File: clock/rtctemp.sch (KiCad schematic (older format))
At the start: 17 parts, among them U601 ADT7410, U602 DS3231, U603 ADT7410

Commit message: Checkpoint layout. Update hand soldering footprints for 0805 parts.
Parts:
- C601, C602, C603: footprint Capacitors_SMD:C_0805_HandSoldering -> local:C_0805_HandSoldering
- R601, R602, R603, R604, R605, R606, R607, R608, R609, R610: footprint Resistors_SMD:R_0805_HandSoldering -> local:R_0805_HandSoldering
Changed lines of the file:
@@
 F 0 "R603" V 4130 2050 50  0000 C CNN
 F 1 "1.00K" V 3975 2050 50  0000 C CNN
-F 2 "Resistors_SMD:R_0805_HandSoldering" V 3980 2050 30  0001 C CNN
+F 2 "local:R_0805_HandSoldering" V 3980 2050 30  0001 C CNN
 F 3 "" V 4130 2050 30  0000 C CNN
 F 4 "1%" V 3900 2050 50  0000 C CNN "Tolerance"
@@
 F 0 "R604" V 4580 2050 50  0000 C CNN
 F 1 "1.00K" V 4425 2050 50  0000 C CNN
-F 2 "Resistors_SMD:R_0805_HandSoldering" V 4430 2050 30  0001 C CNN
+F 2 "local:R_0805_HandSoldering" V 4430 2050 30  0001 C CNN
 F 3 "" V 4580 2050 30  0000 C CNN
 F 4 "1%" V 4350 2050 50  0000 C CNN "Tolerance"
@@
 F 0 "R605" V 5630 4250 50  0000 C CNN
 F 1 "1.00K" V 5475 4250 50  0000 C CNN
-F 2 "Resistors_SMD:R_0805_HandSoldering" V 5480 4250 30  0001 C CNN
+F 2 "local:R_0805_HandSoldering" V 5480 4250 30  0001 C CNN
 F 3 "" V 5630 4250 30  0000 C CNN
 F 4 "1%" V 5400 4250 50  0000 C CNN "Tolerance"
@@
 F 0 "R606" V 6080 4250 50  0000 C CNN
 F 1 "1.00K" V 5925 4250 50  0000 C CNN
-F 2 "Resistors_SMD:R_0805_HandSoldering" V 5930 4250 30  0001 C CNN
+F 2 "local:R_0805_HandSoldering" V 5930 4250 30  0001 C CNN
 F 3 "" V 6080 4250 30  0000 C CNN
 F 4 "1%" V 5850 4250 50  0000 C CNN "Tolerance"
@@
 F 0 "R601" V 3180 5300 50  0000 C CNN
 F 1 "1.00K" V 3025 5300 50  0000 C CNN
-F 2 "Resistors_SMD:R_0805_HandSoldering" V 3030 5300 30  0001 C CNN
+F 2 "local:R_0805_HandSoldering" V 3030 5300 30  0001 C CNN
 F 3 "" V 3180 5300 30  0000 C CNN
 F 4 "1%" V 2950 5300 50  0000 C CNN "Tolerance"
@@
 F 0 "R602" V 3630 5300 50  0000 C CNN
 F 1 "1.00K" V 3475 5300 50  0000 C CNN
-F 2 "Resistors_SMD:R_0805_HandSoldering" V 3480 5300 30  0001 C CNN
+F 2 "local:R_0805_HandSoldering" V 3480 5300 30  0001 C CNN
 F 3 "" V 3630 5300 30  0000 C CNN
 F 4 "1%" V 3400 5300 50  0000 C CNN "Tolerance"
@@
 F 0 "R608" V 6530 5300 50  0000 C CNN
 F 1 "1.00K" V 6375 5300 50  0000 C CNN
-F 2 "Resistors_SMD:R_0805_HandSoldering" V 6380 5300 30  0001 C CNN
+F 2 "local:R_0805_HandSoldering" V 6380 5300 30  0001 C CNN
 F 3 "" V 6530 5300 30  0000 C CNN
 F 4 "1%" V 6300 5300 50  0000 C CNN "Tolerance"
@@
 F 0 "R607" V 6530 4250 50  0000 C CNN
 F 1 "1.00K" V 6375 4250 50  0000 C CNN
-F 2 "Resistors_SMD:R_0805_HandSoldering" V 6380 4250 30  0001 C CNN
+F 2 "local:R_0805_HandSoldering" V 6380 4250 30  0001 C CNN
 F 3 "" V 6530 4250 30  0000 C CNN
 F 4 "1%" V 6300 4250 50  0000 C CNN "Tolerance"
@@
 F 0 "C603" H 8575 2600 50  0000 L CNN
 F 1 "0.1uF" H 8575 2400 50  0000 L CNN
-F 2 "Capacitors_SMD:C_0805_HandSoldering" H 8588 2350 30  0001 C CNN
+F 2 "local:C_0805_HandSoldering" H 8588 2350 30  0001 C CNN
 F 3 "" H 8550 2500 60  0000 C CNN
 F 4 "50V" H 8450 2400 50  0000 C CNN "Voltage"
@@
 F 0 "C601" H 4175 6450 50  0000 L CNN
 F 1 "0.1uF" H 4175 6250 50  0000 L CNN
-F 2 "Capacitors_SMD:C_0805_HandSoldering" H 4188 6200 30  0001 C CNN
+F 2 "local:C_0805_HandSoldering" H 4188 6200 30  0001 C CNN
 F 3 "" H 4150 6350 60  0000 C CNN
 F 4 "50V" H 4050 6250 50  0000 C CNN "Voltage"
@@
 F 0 "C602" H 6175 6450 50  0000 L CNN
 F 1 "0.1uF" H 6175 6250 50  0000 L CNN
-F 2 "Capacitors_SMD:C_0805_HandSoldering" H 6188 6200 30  0001 C CNN
+F 2 "local:C_0805_HandSoldering" H 6188 6200 30  0001 C CNN
 F 3 "" H 6150 6350 60  0000 C CNN
 F 4 "50V" H 6050 6250 50  0000 C CNN "Voltage"
@@
 F 0 "R609" V 6580 1450 50  0000 C CNN
 F 1 "10.0K" V 6425 1450 50  0000 C CNN
-F 2 "Resistors_SMD:R_0805_HandSoldering" V 6430 1450 30  0001 C CNN
+F 2 "local:R_0805_HandSoldering" V 6430 1450 30  0001 C CNN
 F 3 "" V 6580 1450 30  0000 C CNN
 F 4 "1%" V 6350 1450 50  0000 C CNN "Tolerance"
@@
 F 0 "R610" V 7130 1450 50  0000 C CNN
 F 1 "10.0K" V 6975 1450 50  0000 C CNN
-F 2 "Resistors_SMD:R_0805_HandSoldering" V 6980 1450 30  0001 C CNN
+F 2 "local:R_0805_HandSoldering" V 6980 1450 30  0001 C CNN
 F 3 "" V 7130 1450 30  0000 C CNN
 F 4 "1%" V 6900 1450 50  0000 C CNN "Tolerance"

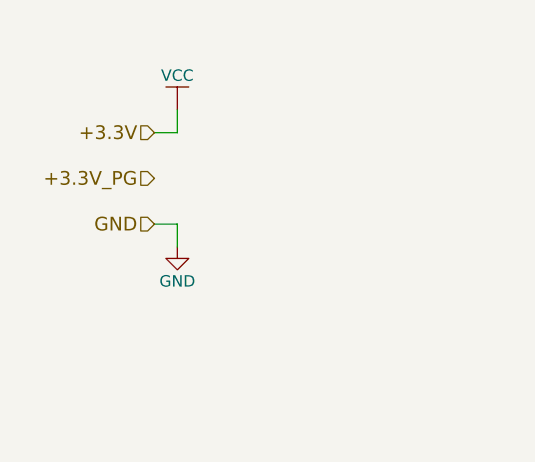
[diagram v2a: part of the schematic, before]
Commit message: Remove sheet to sheet power interconnect because power symbols are global.
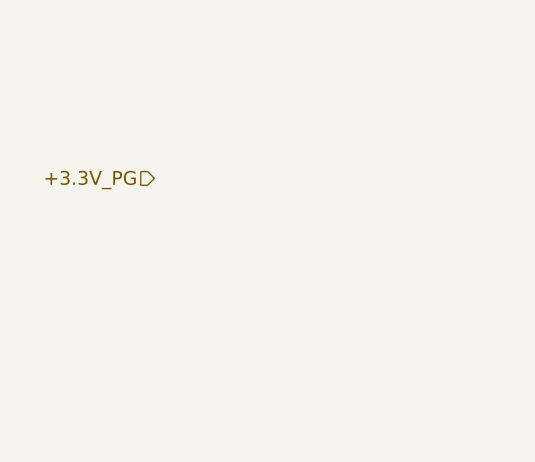
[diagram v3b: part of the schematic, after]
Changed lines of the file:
@@
 	1    0    0    -1
 $EndComp
-Text HLabel 1350 1400 0    60   Input ~ 0
-+3.3V
 Text HLabel 1350 1600 0    60   Input ~ 0
 +3.3V_PG
-Text HLabel 1350 1800 0    60   Input ~ 0
-GND
 Text HLabel 3650 2350 0    60   Input ~ 0
 RTC_SCL
 Text HLabel 3650 2450 0    60   Input ~ 0
 RTC_SDA
-$Comp
-L GND #PWR083
-U 1 1 5636B600
-P 1450 1900
-F 0 "#PWR083" H 1450 1650 50  0001 C CNN
-F 1 "GND" H 1450 1750 50  0000 C CNN
-F 2 "" H 1450 1900 60  0000 C CNN
-F 3 "" H 1450 1900 60  0000 C CNN
-	1    1450 1900
-	1    0    0    -1
-$EndComp
-Wire Wire Line
-	1350 1800 1450 1800
-Wire Wire Line
-	1450 1800 1450 1900
 Wire Wire Line
 	5750 3400 5750 3300
 $Comp
-L GND #PWR084
+L GND #PWR081
 U 1 1 5636B6C4
 P 5750 3400
-F 0 "#PWR084" H 5750 3150 50  0001 C CNN
+F 0 "#PWR081" H 5750 3150 50  0001 C CNN
 F 1 "GND" H 5750 3250 50  0000 C CNN
 F 2 "" H 5750 3400 60  0000 C CNN
@@
 $EndComp
 $Comp
-L VCC #PWR085
-U 1 1 5636B791
-P 1450 1300
-F 0 "#PWR085" H 1450 1150 50  0001 C CNN
-F 1 "VCC" H 1450 1450 50  0000 C CNN
-F 2 "" H 1450 1300 60  0000 C CNN
-F 3 "" H 1450 1300 60  0000 C CNN
-	1    1450 1300
-	1    0    0    -1
-$EndComp
-Wire Wire Line
-	1350 1400 1450 1400
-Wire Wire Line
-	1450 1400 1450 1300
-$Comp
-L VCC #PWR086
+L VCC #PWR082
 U 1 1 5636B7D2
 P 5750 2000
-F 0 "#PWR086" H 5750 1850 50  0001 C CNN
+F 0 "#PWR082" H 5750 1850 50  0001 C CNN
 F 1 "VCC" H 5750 2150 50  0000 C CNN
 F 2 "" H 5750 2000 60  0000 C CNN
@@
 	4500 1800 4500 1900
 $Comp
-L VCC #PWR087
+L VCC #PWR083
 U 1 1 5636BBAE
 P 4300 1700
-F 0 "#PWR087" H 4300 1550 50  0001 C CNN
+F 0 "#PWR083" H 4300 1550 50  0001 C CNN
 F 1 "VCC" H 4300 1850 50  0000 C CNN
 F 2 "" H 4300 1700 60  0000 C CNN
@@
 	6950 2550 6950 2650
 $Comp
-L GND #PWR088
+L GND #PWR084
 U 1 1 5636BC94
 P 6950 3050
-F 0 "#PWR088" H 6950 2800 50  0001 C CNN
+F 0 "#PWR084" H 6950 2800 50  0001 C CNN
 F 1 "GND" H 6950 2900 50  0000 C CNN
 F 2 "" H 6950 3050 60  0000 C CNN
@@
 $EndComp
 $Comp
-L VCC #PWR089
+L VCC #PWR085
 U 1 1 5636C0D5
 P 4200 4150
-F 0 "#PWR089" H 4200 4000 50  0001 C CNN
+F 0 "#PWR085" H 4200 4000 50  0001 C CNN
 F 1 "VCC" H 4200 4300 50  0000 C CNN
 F 2 "" H 4200 4150 60  0000 C CNN
@@
 	7100 5350 7100 5250
 $Comp
-L GND #PWR090
+L GND #PWR086
 U 1 1 5636C104
 P 7100 5350
-F 0 "#PWR090" H 7100 5100 50  0001 C CNN
+F 0 "#PWR086" H 7100 5100 50  0001 C CNN
 F 1 "GND" H 7100 5200 50  0000 C CNN
 F 2 "" H 7100 5350 60  0000 C CNN
@@
 	4200 5350 4200 5250
 $Comp
-L GND #PWR091
+L GND #PWR087
 U 1 1 5636C11B
 P 4200 5350
-F 0 "#PWR091" H 4200 5100 50  0001 C CNN
+F 0 "#PWR087" H 4200 5100 50  0001 C CNN
 F 1 "GND" H 4200 5200 50  0000 C CNN
 F 2 "" H 4200 5350 60  0000 C CNN
@@
 	6000 4000 6000 4100
 $Comp
-L VCC #PWR092
+L VCC #PWR088
 U 1 1 5636C1AA
 P 5800 3900
-F 0 "#PWR092" H 5800 3750 50  0001 C CNN
+F 0 "#PWR088" H 5800 3750 50  0001 C CNN
 F 1 "VCC" H 5800 4050 50  0000 C CNN
 F 2 "" H 5800 3900 60  0000 C CNN
@@
 Connection ~ 3550 5550
 $Comp
-L GND #PWR093
+L GND #PWR089
 U 1 1 5636C550
 P 3550 5650
-F 0 "#PWR093" H 3550 5400 50  0001 C CNN
+F 0 "#PWR089" H 3550 5400 50  0001 C CNN
 F 1 "GND" H 3550 5500 50  0000 C CNN
 F 2 "" H 3550 5650 60  0000 C CNN
@@
 	6450 4950 6450 5150
 $Comp
-L GND #PWR094
+L GND #PWR090
 U 1 1 5636C5CD
 P 6450 5550
-F 0 "#PWR094" H 6450 5300 50  0001 C CNN
+F 0 "#PWR090" H 6450 5300 50  0001 C CNN
 F 1 "GND" H 6450 5400 50  0000 C CNN
 F 2 "" H 6450 5550 60  0000 C CNN
@@
 Connection ~ 3500 4650
 $Comp
-L GND #PWR095
+L GND #PWR091
 U 1 1 5636CF30
 P 8550 2750
-F 0 "#PWR095" H 8550 2500 50  0001 C CNN
+F 0 "#PWR091" H 8550 2500 50  0001 C CNN
 F 1 "GND" H 8550 2600 50  0000 C CNN
 F 2 "" H 8550 2750 60  0000 C CNN
@@
 $EndComp
 $Comp
-L VCC #PWR096
+L VCC #PWR092
 U 1 1 5636D2DE
 P 8550 2250
-F 0 "#PWR096" H 8550 2100 50  0001 C CNN
+F 0 "#PWR092" H 8550 2100 50  0001 C CNN
 F 1 "VCC" H 8550 2400 50  0000 C CNN
 F 2 "" H 8550 2250 60  0000 C CNN
@@
 $EndComp
 $Comp
-L GND #PWR097
+L GND #PWR093
 U 1 1 5636D43C
 P 4150 6600
-F 0 "#PWR097" H 4150 6350 50  0001 C CNN
+F 0 "#PWR093" H 4150 6350 50  0001 C CNN
 F 1 "GND" H 4150 6450 50  0000 C CNN
 F 2 "" H 4150 6600 60  0000 C CNN
@@
 $EndComp
 $Comp
-L VCC #PWR098
+L VCC #PWR094
 U 1 1 5636D44F
 P 4150 6100
-F 0 "#PWR098" H 4150 5950 50  0001 C CNN
+F 0 "#PWR094" H 4150 5950 50  0001 C CNN
 F 1 "VCC" H 4150 6250 50  0000 C CNN
 F 2 "" H 4150 6100 60  0000 C CNN
@@
 $EndComp
 $Comp
-L GND #PWR099
+L GND #PWR095
 U 1 1 5636D49F
 P 6150 6600
-F 0 "#PWR099" H 6150 6350 50  0001 C CNN
+F 0 "#PWR095" H 6150 6350 50  0001 C CNN
 F 1 "GND" H 6150 6450 50  0000 C CNN
 F 2 "" H 6150 6600 60  0000 C CNN
@@
 $EndComp
 $Comp
-L VCC #PWR0100
+L VCC #PWR096
 U 1 1 5636D4B2
 P 6150 6100
-F 0 "#PWR0100" H 6150 5950 50  0001 C CNN
+F 0 "#PWR096" H 6150 5950 50  0001 C CNN
 F 1 "VCC" H 6150 6250 50  0000 C CNN
 F 2 "" H 6150 6100 60  0000 C CNN
@@
 NoConn ~ 5150 2550
 $Comp
-L VCC #PWR0101
+L VCC #PWR097
 U 1 1 563E1DA8
 P 7100 4150
-F 0 "#PWR0101" H 7100 4000 50  0001 C CNN
+F 0 "#PWR097" H 7100 4000 50  0001 C CNN
 F 1 "VCC" H 7100 4300 50  0000 C CNN
 F 2 "" H 7100 4150 60  0000 C CNN
@@
 	6450 5550 6450 5450
 $Comp
-L PWR_FLAG #FLG0102
+L PWR_FLAG #FLG098
 U 1 1 564556C2
 P 7300 2450
-F 0 "#FLG0102" H 7300 2545 50  0001 C CNN
+F 0 "#FLG098" H 7300 2545 50  0001 C CNN
 F 1 "PWR_FLAG" H 7300 2630 50  0000 C CNN
 F 2 "" H 7300 2450 60  0000 C CNN
@@
 Connection ~ 6500 1700
 $Comp
-L VCC #PWR0103
+L VCC #PWR099
 U 1 1 57AC17FC
 P 7050 1100
-F 0 "#PWR0103" H 7050 950 50  0001 C CNN
+F 0 "#PWR099" H 7050 950 50  0001 C CNN
 F 1 "VCC" H 7050 1250 50  0000 C CNN
 F 2 "" H 7050 1100 60  0000 C CNN

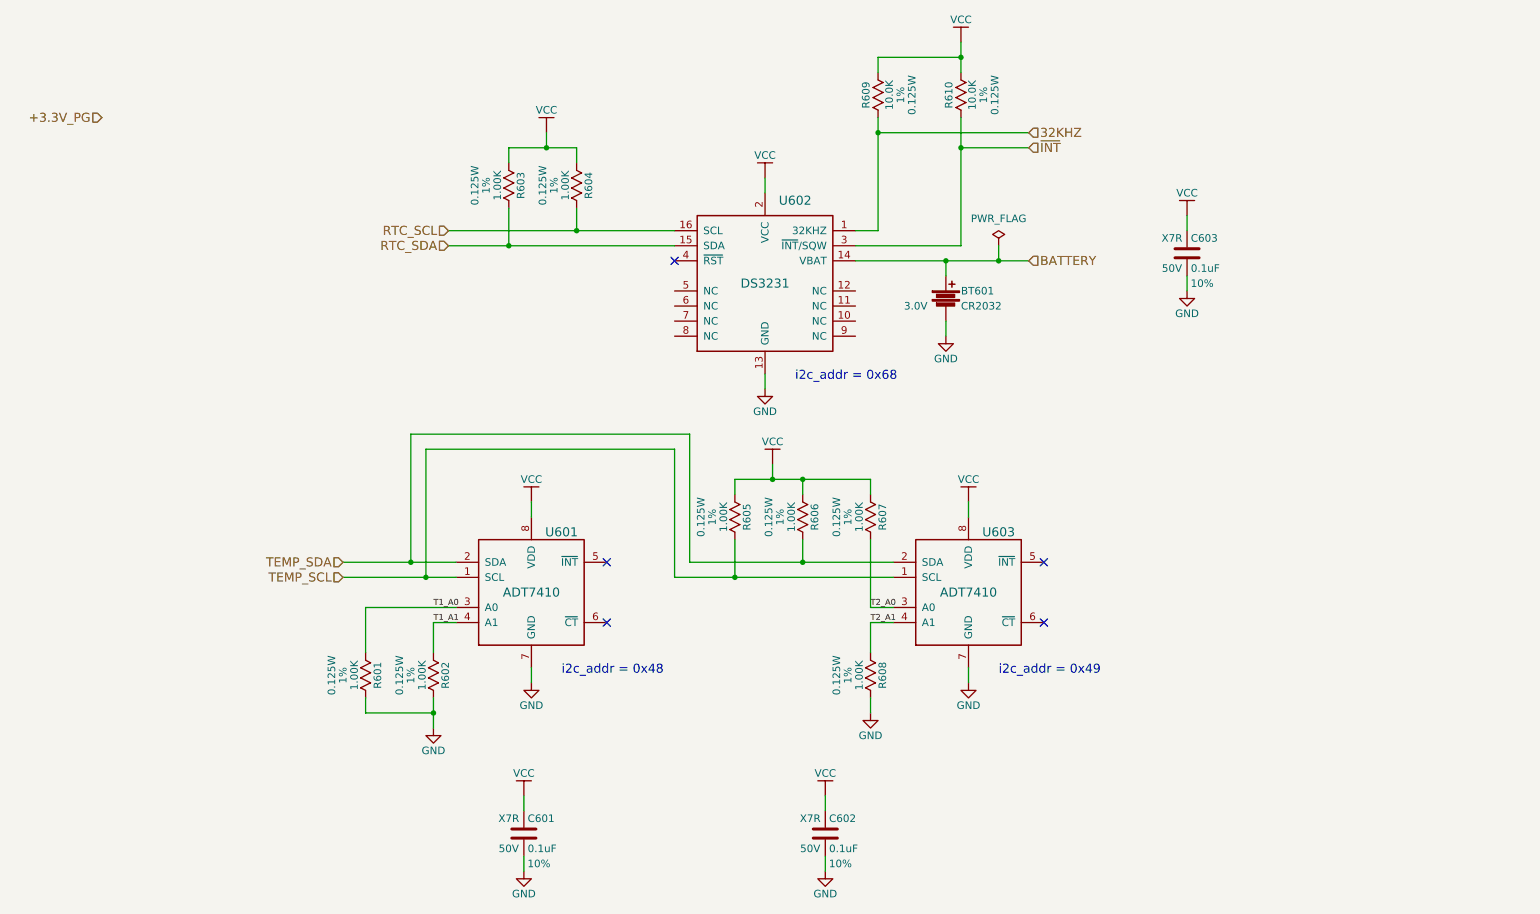
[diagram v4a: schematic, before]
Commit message: Connect temperature sensor interrupt to FPGA.
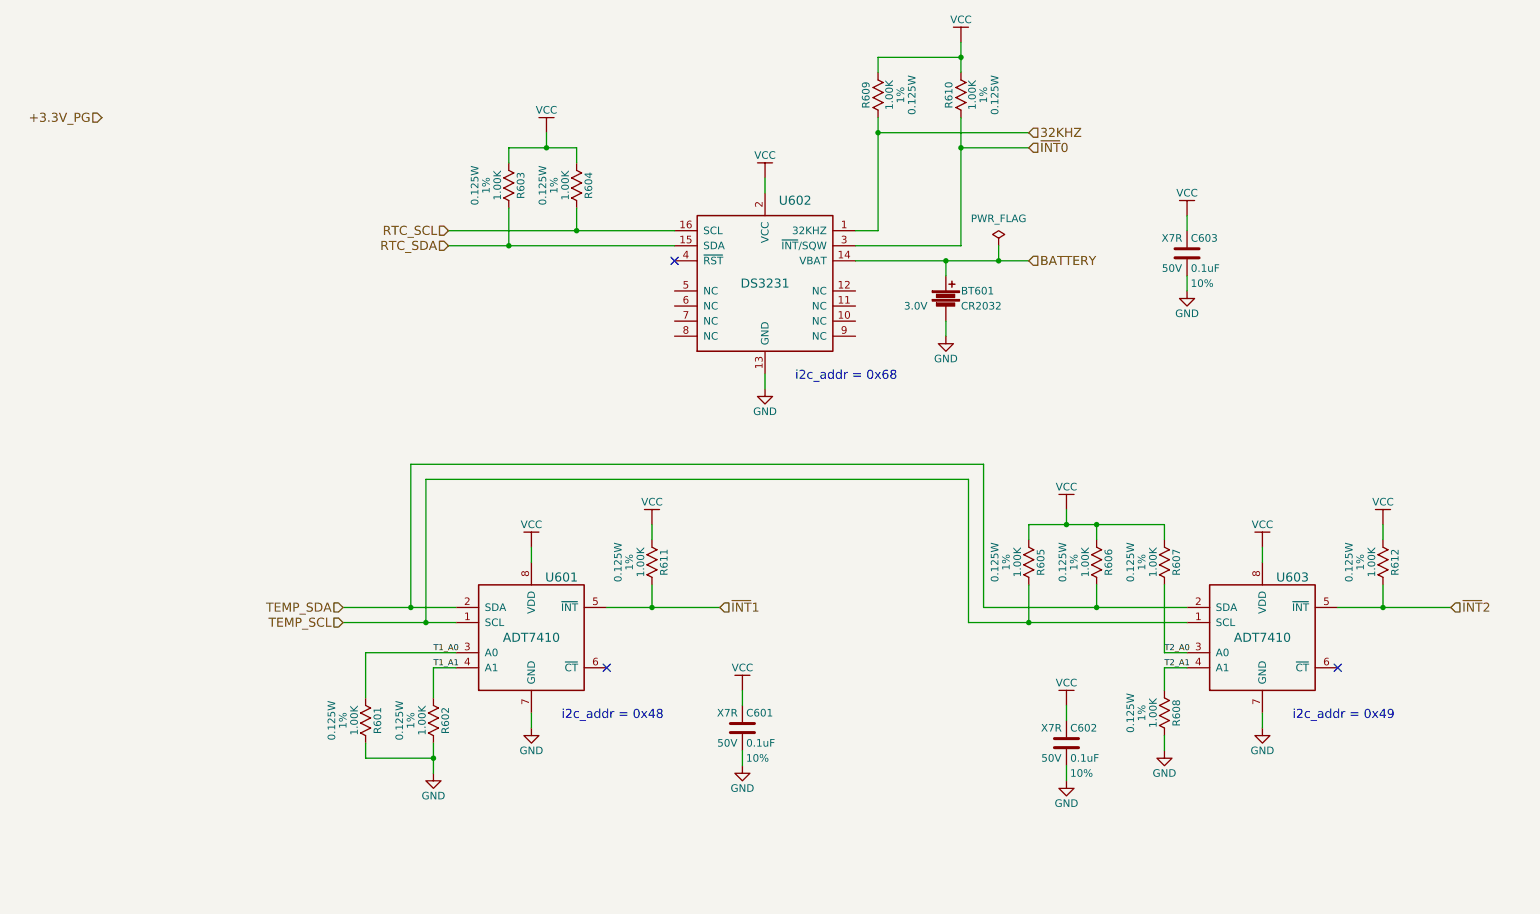
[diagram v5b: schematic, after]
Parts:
- added R611, R612: 1.00K, local:R_0805_HandSoldering, symbol R_local
- R609, R610: value 10.0K -> 1.00K; PartNum CRCW080510K0FKEA -> CRCW08051K00FKEA
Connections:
- net VCC: now also R611.1, R612.1
- net ~INT~1: now reaches U601.5 (~INT~)
- net ~INT~1: now also R611.2
- net ~INT~2: now reaches U603.5 (~INT~)
- net ~INT~2: now also R612.2
- net ~INT~ renamed ~INT~0
- no-connect marks 5 -> 3
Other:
- moved on the sheet: C601, C602, R601, R602, R605, R606, R607, R608, U601, U603

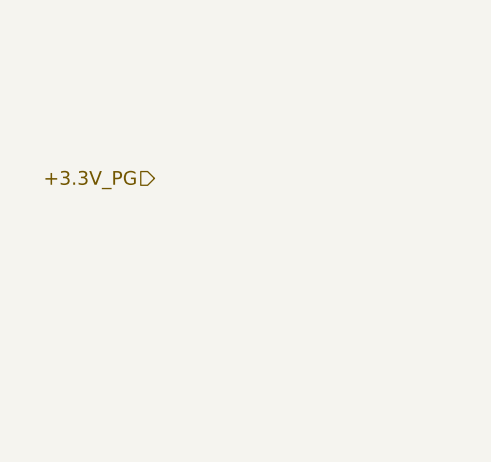
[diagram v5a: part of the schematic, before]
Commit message: Change schematic values to "as built". Regenerate pdf schematic.
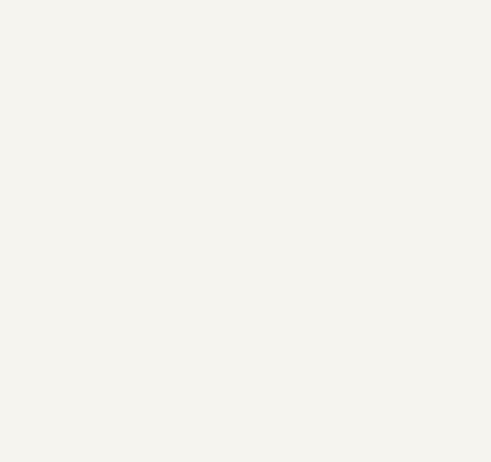
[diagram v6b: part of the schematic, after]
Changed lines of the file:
@@
 	1    0    0    -1
 $EndComp
-Text HLabel 1350 1600 0    60   Input ~ 0
-+3.3V_PG
 Text HLabel 3650 2350 0    60   Input ~ 0
 RTC_SCL

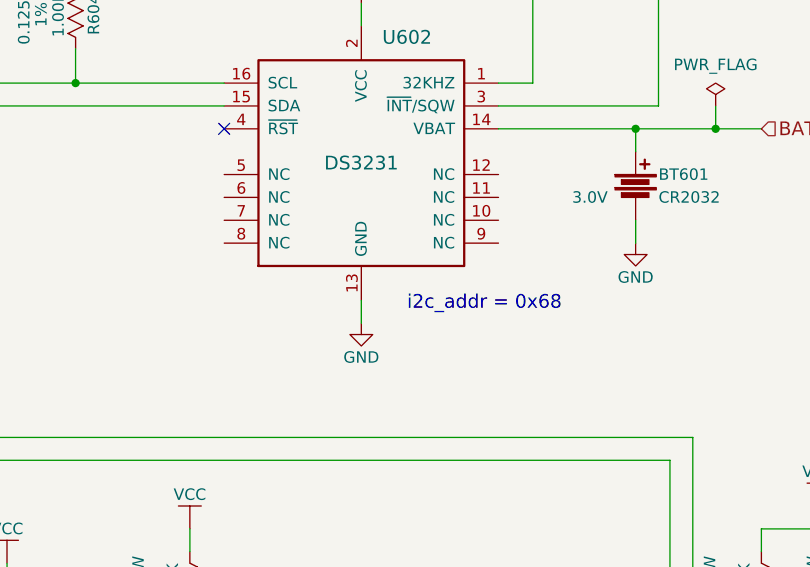
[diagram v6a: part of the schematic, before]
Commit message: Minor untested updates. Ground the NC pins on the RTC.
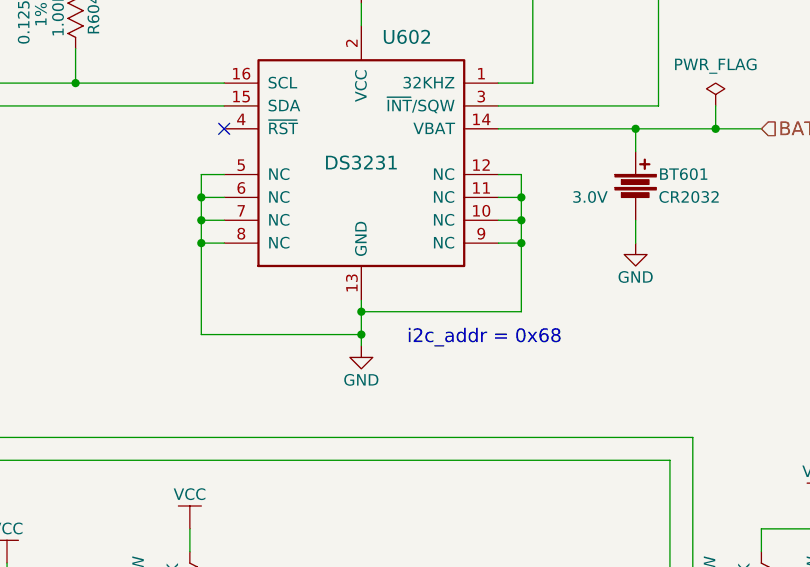
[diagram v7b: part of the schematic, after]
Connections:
- net GND: now also U602.10 (NC), U602.11 (NC), U602.12 (NC), U602.5 (NC), U602.6 (NC), U602.7 (NC), U602.8 (NC), U602.9 (NC)
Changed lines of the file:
@@
 EESchema Schematic File Version 2
+LIBS:clock-rescue
 LIBS:local
 LIBS:power
@@
 U 1 1 5636A7B6
 P 5750 2700
+AR Path="/5636A7B6" Ref="U602"  Part="1"
+AR Path="/5636A673/5636A7B6" Ref="U602"  Part="1"
 F 0 "U602" H 5950 3250 60  0000 C CNN
 F 1 "DS3231" H 5750 2700 60  0000 C CNN
@@
 RTC_SDA
 Wire Wire Line
-	5750 3400 5750 3300
+	5750 3300 5750 3500
 $Comp
 L GND #PWR082
 U 1 1 5636B6C4
-P 5750 3400
-F 0 "#PWR082" H 5750 3150 50  0001 C CNN
-F 1 "GND" H 5750 3250 50  0000 C CNN
-F 2 "" H 5750 3400 60  0000 C CNN
-F 3 "" H 5750 3400 60  0000 C CNN
-	1    5750 3400
+P 5750 3500
+F 0 "#PWR082" H 5750 3250 50  0001 C CNN
+F 1 "GND" H 5750 3350 50  0000 C CNN
+F 2 "" H 5750 3500 60  0000 C CNN
+F 3 "" H 5750 3500 60  0000 C CNN
+	1    5750 3500
 	1    0    0    -1
 $EndComp
@@
 $EndComp
 Connection ~ 7050 1200
-Text Notes 5950 3350 0    60   ~ 0
+Text Notes 5950 3500 0    60   ~ 0
 i2c_addr = 0x68
 Text Notes 4400 5600 0    60   ~ 0
@@
 ~INT~2
 Connection ~ 9850 4850
+Wire Wire Line
+	5150 2750 5050 2750
+Wire Wire Line
+	5050 2750 5050 3450
+Wire Wire Line
+	5050 3450 5750 3450
+Wire Wire Line
+	5150 2850 5050 2850
+Connection ~ 5050 2850
+Wire Wire Line
+	5150 2950 5050 2950
+Connection ~ 5050 2950
+Wire Wire Line
+	5150 3050 5050 3050
+Connection ~ 5050 3050
+Wire Wire Line
+	6450 3350 5750 3350
+Wire Wire Line
+	6450 2750 6450 3350
+Wire Wire Line
+	6450 2750 6350 2750
+Connection ~ 5750 3350
+Wire Wire Line
+	6350 2850 6450 2850
+Connection ~ 6450 2850
+Wire Wire Line
+	6450 2950 6350 2950
+Connection ~ 6450 2950
+Wire Wire Line
+	6350 3050 6450 3050
+Connection ~ 6450 3050
+Connection ~ 5750 3450
 $EndSCHEMATC
